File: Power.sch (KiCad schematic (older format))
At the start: 32 parts, among them J14 Conn_01x02, Q5 AO3401A, U3 TPS54228, U4 TPS54228

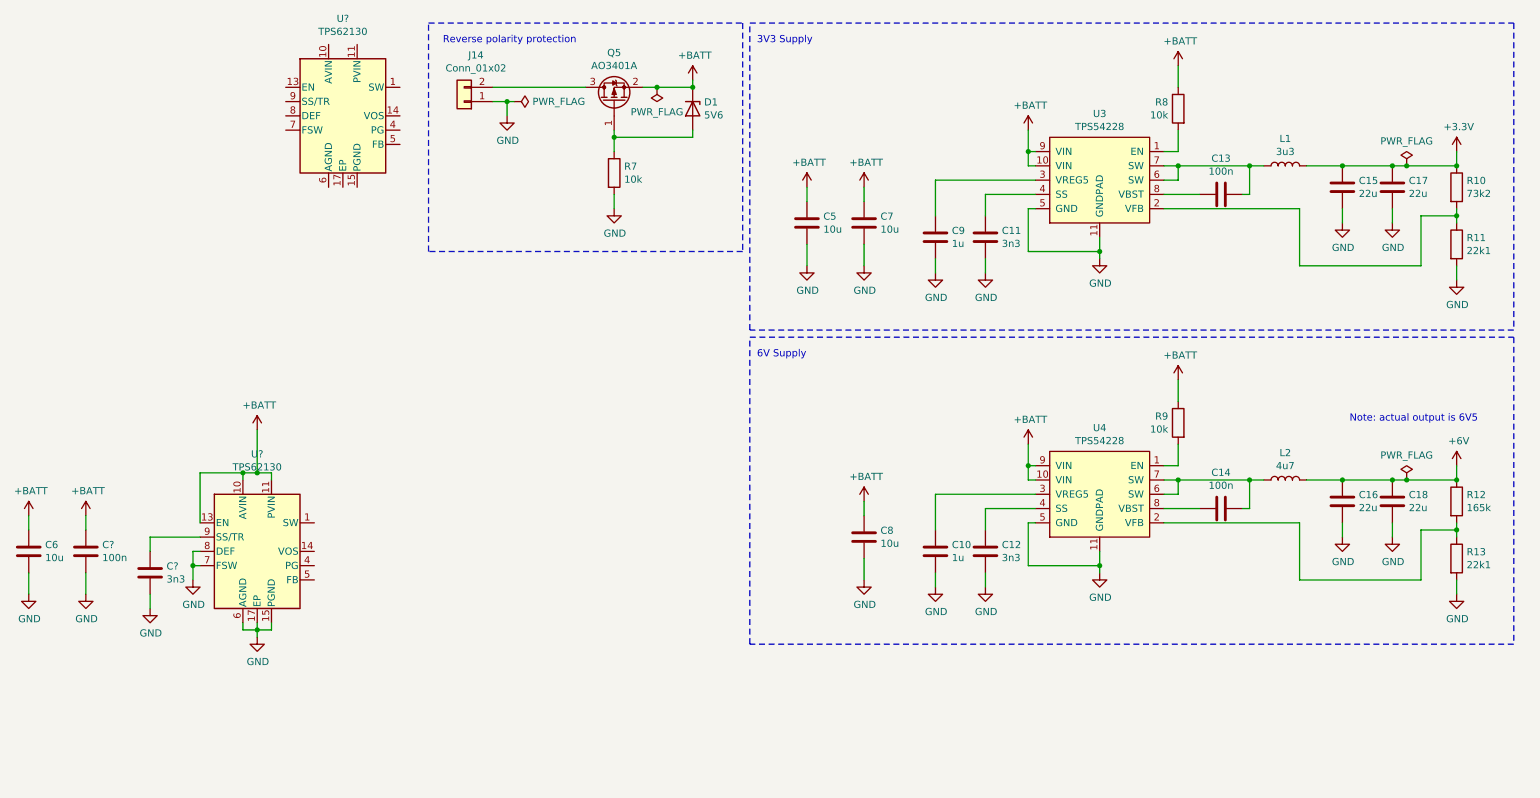
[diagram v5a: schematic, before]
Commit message: Finished revising power section schematic
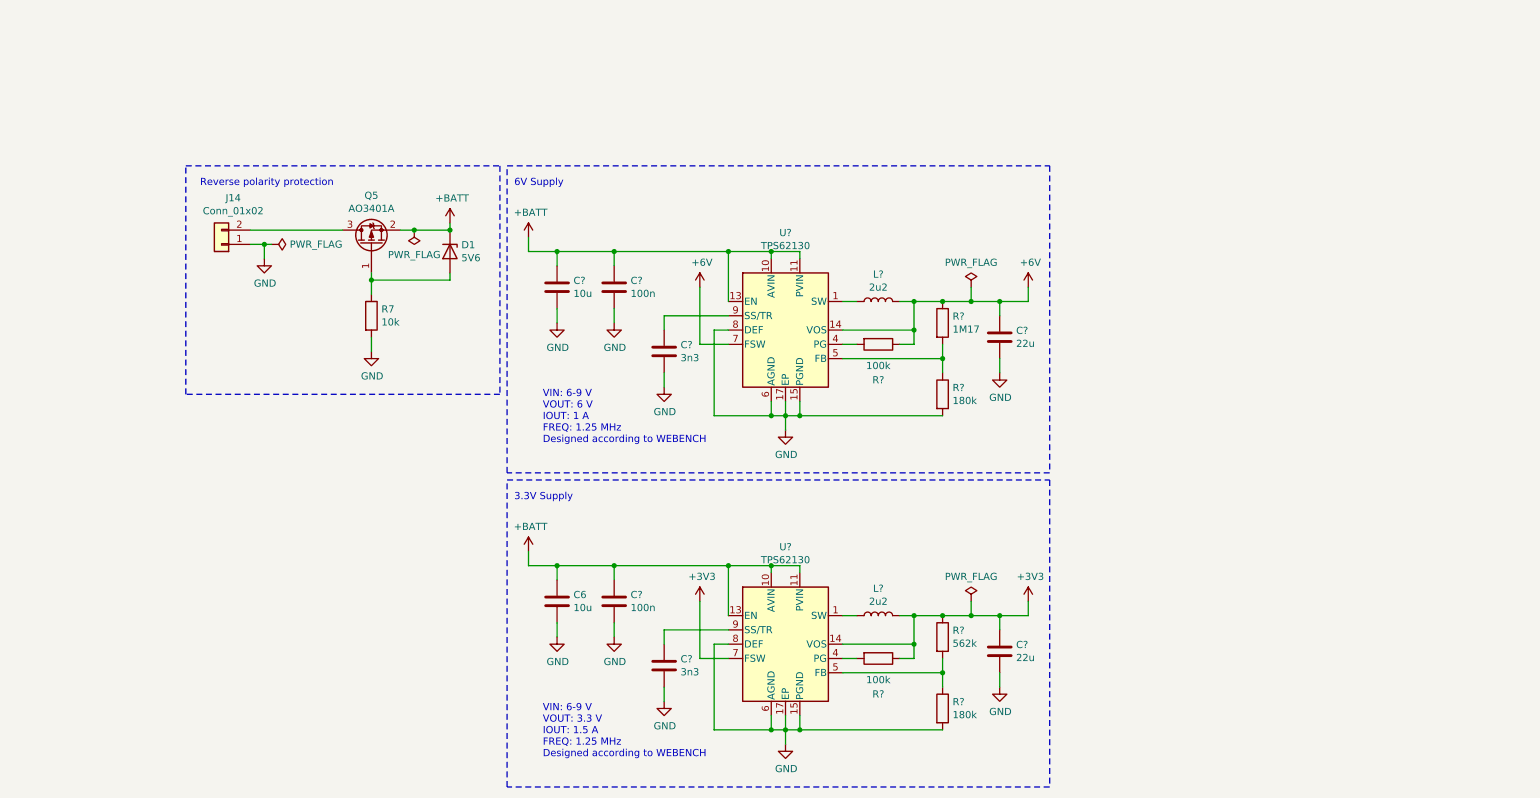
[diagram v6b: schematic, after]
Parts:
- removed C10, C9: 1u, Capacitor_SMD:C_0603_1608Metric, symbol Device:C
- removed C11, C12: 3n3, Capacitor_SMD:C_0603_1608Metric, symbol Device:C
- removed C13, C14: 100n, Capacitor_SMD:C_0603_1608Metric, symbol Device:C
- removed C15, C16, C17, C18: 22u, Capacitor_SMD:C_0805_2012Metric, symbol Device:C
- removed C5, C7, C8: 10u, Capacitor_SMD:C_0805_2012Metric, symbol Device:C
- removed L1: 3u3, co2_sensor_node:YP0403, symbol Device:L
- removed L2: 4u7, co2_sensor_node:WPN4020, symbol Device:L
- removed R10: 73k2, Resistor_SMD:R_0603_1608Metric, symbol Device:R
- removed R11, R13: 22k1, Resistor_SMD:R_0603_1608Metric, symbol Device:R
- removed R12: 165k, Resistor_SMD:R_0603_1608Metric, symbol Device:R
- removed R8, R9: 10k, Resistor_SMD:R_0603_1608Metric, symbol Device:R
- removed U3, U4: TPS54228, Package_SON:VSON-10-1EP_3x3mm_P0.5mm_EP1.2x2mm, symbol co2_sensor_node:TPS54228
- removed U?: TPS62130, Package_DFN_QFN:VQFN-16-1EP_3x3mm_P0.5mm_EP1.68x1.68mm_ThermalVias, symbol Regulator_Switching:TPS62130
- added C? (x2): 22u, symbol Device:C
- added C?: 10u, Capacitor_SMD:C_0805_2012Metric, symbol Device:C
- added C?: 100n, symbol Device:C
- added C?: 3n3, symbol Device:C
- added L? (x2): 2u2, symbol Device:L
- added R? (x2): 100k, symbol Device:R
- added R? (x2): 180k, symbol Device:R
- added R?: 562k, symbol Device:R
- added R?: 1M17, symbol Device:R
- added U?: TPS62130, Package_DFN_QFN:VQFN-16-1EP_3x3mm_P0.5mm_EP1.68x1.68mm_ThermalVias, symbol Regulator_Switching:TPS62130
- U?: LCSC (none) -> C43590
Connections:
- net +3V3: now also U?.14 (VOS), U?.7 (FSW), C?.1, L?.2, R?.1, R?.1
- net +6V: now also C?.1, L?.2, R?.1, R?.1, U?.14 (VOS), U?.7 (FSW)
- net +BATT: now also C?.1, C?.1, U?.10 (AVIN), U?.11 (PVIN), U?.12 (PVIN), U?.13 (EN)
- net GND: now also C?.2, C?.2, C?.2, C?.2, C?.2, R?.2, R?.2, U?.15 (PGND), U?.16 (PGND), U?.17 (EP), U?.6 (AGND), U?.8 (DEF); no longer U?.7 (FSW)
- net at U?.1 (SW), U?.2 (SW), U?.3 (SW): now also L?.1
- net at U?.4 (PG): now also R?.2
- net at U?.5 (FB): now also R?.1, R?.2
- new net: L?.1, U?.1 (SW), U?.2 (SW), U?.3 (SW)
- new net: R?.2, U?.4 (PG)
- new net: R?.1, R?.2, U?.5 (FB)
- new net: C?.1, U?.9 (SS/TR)
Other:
- note added: "3.3V Supply\n"
- note added: "VIN: 6-9 V\nVOUT: 3.3 V\nIOUT: 1.5 A\nFREQ: 1.25 MHz\nDesigned according to WEBENCH\n"
- note added: "VIN: 6-9 V\nVOUT: 6 V\nIOUT: 1 A\nFREQ: 1.25 MHz\nDesigned according to WEBENCH\n"
- note removed: "3V3 Supply\n"
- note removed: "Note: actual output is 6V5\n"
- moved on the sheet: C6, C?, D1, J14, Q5, R7, U?
